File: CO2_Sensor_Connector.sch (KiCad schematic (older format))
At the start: 7 parts, among them J1 Conn_01x07_Female, J2 Conn_01x04_Female, Q1 AO3400A, Q2 AO3401A

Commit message: Finalize schematic
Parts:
- removed J1: Conn_01x07_Female, Connector_PinSocket_2.54mm:PinSocket_1x07_P2.54mm_Vertical, symbol Connector:Conn_01x07_Female
- removed J2: Conn_01x04_Female, Connector_PinSocket_2.54mm:PinSocket_1x04_P2.54mm_Vertical, symbol Connector:Conn_01x04_Female
- added J?: Conn_01x04, Connector_JST:JST_XH_S4B-XH-A_1x04_P2.50mm_Horizontal, symbol Connector_Generic:Conn_01x04
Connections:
- net GND: now also J?.4 (Pin_4)
- net UART_RX: now also J?.2 (Pin_2)
- net UART_TX: now also J?.1 (Pin_1)
- net VCC: now also J?.3 (Pin_3)
- no-connect marks 1 -> 0
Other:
- note removed: "Connector for SCD30"
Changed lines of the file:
@@
 Comment4 ""
 $EndDescr
-Text HLabel 6000 3900 2    50   Input ~ 0
-UART_RX
-Text HLabel 6000 3800 2    50   Output ~ 0
-UART_TX
 Text HLabel 3300 4200 0    50   Input ~ 0
 ENABLE
-Text HLabel 6000 4000 2    50   Output ~ 0
-N_RDY
-$Comp
-L Connector:Conn_01x07_Female J1
-U 1 1 60A57B40
-P 5800 3900
-AR Path="/60A49A7C/60A57B40" Ref="J1"  Part="1"
-AR Path="/60A4AC4A/60A57B40" Ref="J3"  Part="1"
-F 0 "J1" H 5692 4385 50  0000 C CNN
-F 1 "Conn_01x07_Female" H 5692 4294 50  0000 C CNN
-F 2 "Connector_PinSocket_2.54mm:PinSocket_1x07_P2.54mm_Vertical" H 5800 3900 50  0001 C CNN
-F 3 "~" H 5800 3900 50  0001 C CNN
-F 4 "C358721" H 5800 3900 50  0001 C CNN "LCSC"
-	1    5800 3900
-	-1   0    0    -1
-$EndComp
 Text Notes 7200 4350 0    50   ~ 0
 Connector for K30
-Text Notes 5600 4350 0    50   ~ 0
-Connector for SCD30
-Wire Wire Line
-	6400 3600 6000 3600
-$Comp
-L power:GND #PWR04
-U 1 1 60A5D6A7
-P 6500 4300
-AR Path="/60A49A7C/60A5D6A7" Ref="#PWR04"  Part="1"
-AR Path="/60A4AC4A/60A5D6A7" Ref="#PWR09"  Part="1"
-F 0 "#PWR04" H 6500 4050 50  0001 C CNN
-F 1 "GND" H 6505 4127 50  0000 C CNN
-F 2 "" H 6500 4300 50  0001 C CNN
-F 3 "" H 6500 4300 50  0001 C CNN
-	1    6500 4300
-	1    0    0    -1
-$EndComp
-Wire Wire Line
-	6500 4300 6500 3700
-Wire Wire Line
-	6000 3700 6500 3700
-Wire Wire Line
-	6000 4200 6400 4200
-Wire Wire Line
-	6400 4200 6400 3600
 $Comp
 L Transistor_FET:AO3401A Q2
@@
 	1    0    0    -1
 $EndComp
-$Comp
-L Connector:Conn_01x04_Female J2
-U 1 1 60ABE2B1
-P 7400 3700
-AR Path="/60A49A7C/60ABE2B1" Ref="J2"  Part="1"
-AR Path="/60A4AC4A/60ABE2B1" Ref="J4"  Part="1"
-F 0 "J2" H 7292 3985 50  0000 C CNN
-F 1 "Conn_01x04_Female" H 7292 3894 50  0000 C CNN
-F 2 "Connector_PinSocket_2.54mm:PinSocket_1x04_P2.54mm_Vertical" H 7400 3700 50  0001 C CNN
-F 3 "~" H 7400 3700 50  0001 C CNN
-	1    7400 3700
-	-1   0    0    -1
-$EndComp
-Wire Wire Line
-	6400 3600 6700 3600
-Connection ~ 6400 3600
-Text Label 6700 3600 2    50   ~ 0
-VCC
 Text Label 7900 3800 2    50   ~ 0
 VCC
@@
 Wire Wire Line
 	3800 4200 4000 4200
-NoConn ~ 6000 4100
 Connection ~ 4800 3400
+$Comp
+L Connector_Generic:Conn_01x04 J?
+U 1 1 60D51FD2
+P 7400 3700
+AR Path="/60A49A7C/60D51FD2" Ref="J?"  Part="1"
+AR Path="/60A4AC4A/60D51FD2" Ref="J?"  Part="1"
+F 0 "J?" H 7318 4017 50  0000 C CNN
+F 1 "Conn_01x04" H 7318 3926 50  0000 C CNN
+F 2 "Connector_JST:JST_XH_S4B-XH-A_1x04_P2.50mm_Horizontal" H 7400 3700 50  0001 C CNN
+F 3 "~" H 7400 3700 50  0001 C CNN
+	1    7400 3700
+	-1   0    0    -1
+$EndComp
 $EndSCHEMATC

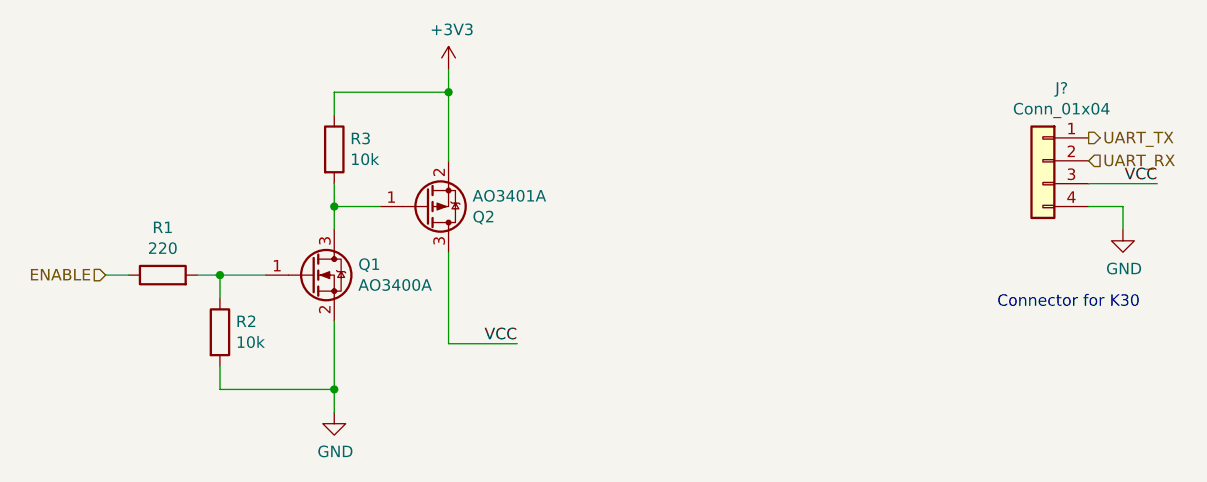
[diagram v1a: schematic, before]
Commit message: Finish routing of Rev 1
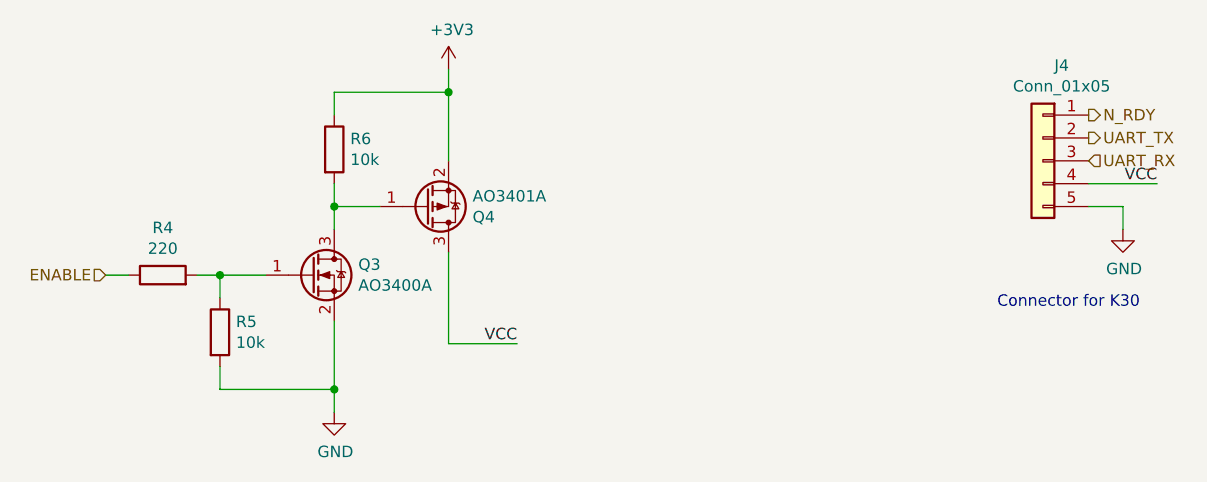
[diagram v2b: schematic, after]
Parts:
- removed J?: Conn_01x04, Connector_JST:JST_XH_S4B-XH-A_1x04_P2.50mm_Horizontal, symbol Connector_Generic:Conn_01x04
- added J3: Conn_01x05, Connector_JST:JST_XH_B5B-XH-AM_1x05_P2.50mm_Vertical, symbol Connector_Generic:Conn_01x05
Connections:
- net GND: now also J3.5 (Pin_5)
- net UART_RX: now also J3.3 (Pin_3)
- net UART_TX: now also J3.2 (Pin_2)
- net VCC: now also J3.4 (Pin_4)
- new net N_RDY: J3.1 (Pin_1)
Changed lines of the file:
@@
 $Descr A4 11693 8268
 encoding utf-8
-Sheet 2 9
+Sheet 3 10
 Title ""
 Date ""
@@
 AR Path="/60A49A7C/60A6C14D" Ref="Q2"  Part="1"
 AR Path="/60A4AC4A/60A6C14D" Ref="Q4"  Part="1"
-F 0 "Q2" H 4905 3946 50  0000 L CNN
+F 0 "Q4" H 4905 3946 50  0000 L CNN
 F 1 "AO3401A" H 4905 3855 50  0000 L CNN
 F 2 "Package_TO_SOT_SMD:SOT-23" H 4900 3825 50  0001 L CIN
@@
 AR Path="/60A49A7C/60A6FA21" Ref="R1"  Part="1"
 AR Path="/60A4AC4A/60A6FA21" Ref="R4"  Part="1"
-F 0 "R1" V 3757 4200 50  0000 C CNN
+F 0 "R4" V 3757 4200 50  0000 C CNN
 F 1 "220" V 3666 4200 50  0000 C CNN
 F 2 "Resistor_SMD:R_0603_1608Metric" V 3480 4200 50  0001 C CNN
@@
 AR Path="/60A49A7C/60A736D3" Ref="R3"  Part="1"
 AR Path="/60A4AC4A/60A736D3" Ref="R6"  Part="1"
-F 0 "R3" H 4370 3696 50  0000 L CNN
+F 0 "R6" H 4370 3696 50  0000 L CNN
 F 1 "10k" H 4370 3605 50  0000 L CNN
 F 2 "Resistor_SMD:R_0603_1608Metric" V 4230 3650 50  0001 C CNN
@@
 AR Path="/60A49A7C/60A94D4D" Ref="#PWR02"  Part="1"
 AR Path="/60A4AC4A/60A94D4D" Ref="#PWR07"  Part="1"
-F 0 "#PWR02" H 4800 3150 50  0001 C CNN
+F 0 "#PWR07" H 4800 3150 50  0001 C CNN
 F 1 "+3V3" H 4815 3473 50  0000 C CNN
 F 2 "" H 4800 3300 50  0001 C CNN
@@
 AR Path="/60A49A7C/60A9EA13" Ref="#PWR01"  Part="1"
 AR Path="/60A4AC4A/60A9EA13" Ref="#PWR06"  Part="1"
-F 0 "#PWR01" H 4300 4550 50  0001 C CNN
+F 0 "#PWR06" H 4300 4550 50  0001 C CNN
 F 1 "GND" H 4305 4627 50  0000 C CNN
 F 2 "" H 4300 4800 50  0001 C CNN
@@
 AR Path="/60A49A7C/60AA508F" Ref="R2"  Part="1"
 AR Path="/60A4AC4A/60AA508F" Ref="R5"  Part="1"
-F 0 "R2" H 3870 4496 50  0000 L CNN
+F 0 "R5" H 3870 4496 50  0000 L CNN
 F 1 "10k" H 3870 4405 50  0000 L CNN
 F 2 "Resistor_SMD:R_0603_1608Metric" V 3730 4450 50  0001 C CNN
@@
 AR Path="/60A49A7C/60ABDE86" Ref="#PWR05"  Part="1"
 AR Path="/60A4AC4A/60ABDE86" Ref="#PWR010"  Part="1"
-F 0 "#PWR05" H 7750 3750 50  0001 C CNN
+F 0 "#PWR010" H 7750 3750 50  0001 C CNN
 F 1 "GND" H 7755 3827 50  0000 C CNN
 F 2 "" H 7750 4000 50  0001 C CNN
@@
 AR Path="/60A49A7C/60B57C20" Ref="Q1"  Part="1"
 AR Path="/60A4AC4A/60B57C20" Ref="Q3"  Part="1"
-F 0 "Q1" H 4405 4246 50  0000 L CNN
+F 0 "Q3" H 4405 4246 50  0000 L CNN
 F 1 "AO3400A" H 4405 4155 50  0000 L CNN
 F 2 "Package_TO_SOT_SMD:SOT-23" H 4400 4125 50  0001 L CIN
@@
 Connection ~ 4800 3400
 $Comp
-L Connector_Generic:Conn_01x04 J?
-U 1 1 60D51FD2
+L Connector_Generic:Conn_01x05 J3
+U 1 1 60D522F2
 P 7400 3700
-AR Path="/60A49A7C/60D51FD2" Ref="J?"  Part="1"
-AR Path="/60A4AC4A/60D51FD2" Ref="J?"  Part="1"
-F 0 "J?" H 7318 4017 50  0000 C CNN
-F 1 "Conn_01x04" H 7318 3926 50  0000 C CNN
-F 2 "Connector_JST:JST_XH_S4B-XH-A_1x04_P2.50mm_Horizontal" H 7400 3700 50  0001 C CNN
+AR Path="/60A49A7C/60D522F2" Ref="J3"  Part="1"
+AR Path="/60A4AC4A/60D522F2" Ref="J4"  Part="1"
+F 0 "J4" H 7318 4117 50  0000 C CNN
+F 1 "Conn_01x05" H 7318 4026 50  0000 C CNN
+F 2 "Connector_JST:JST_XH_B5B-XH-AM_1x05_P2.50mm_Vertical" H 7400 3700 50  0001 C CNN
 F 3 "~" H 7400 3700 50  0001 C CNN
 	1    7400 3700
 	-1   0    0    -1
 $EndComp
+Text HLabel 7600 3500 2    50   Output ~ 0
+N_RDY
 $EndSCHEMATC
